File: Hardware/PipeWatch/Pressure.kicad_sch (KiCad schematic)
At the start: 4 parts, among them U6 ADS1115IDGS

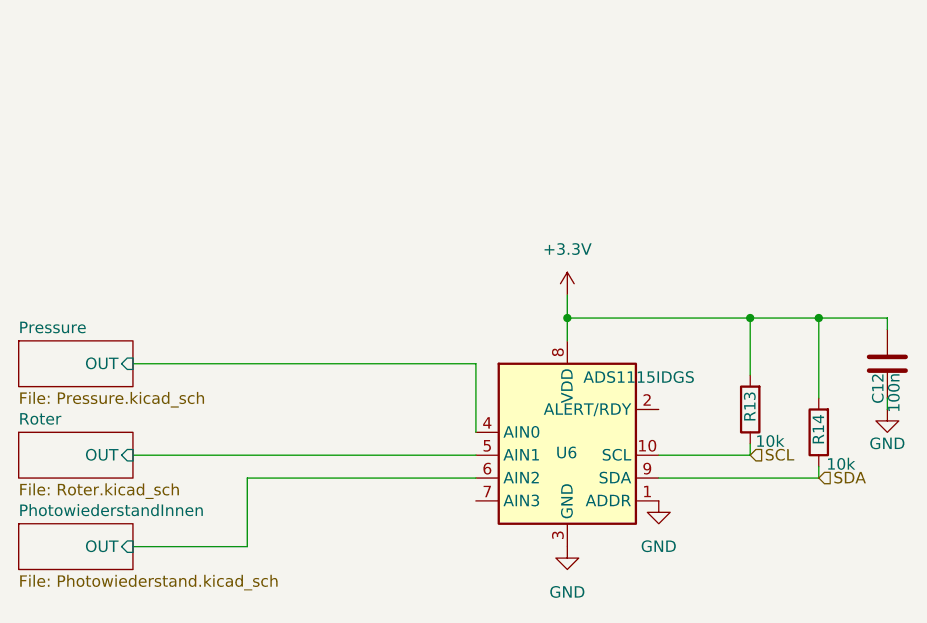
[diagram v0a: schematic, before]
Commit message: Started laying traces
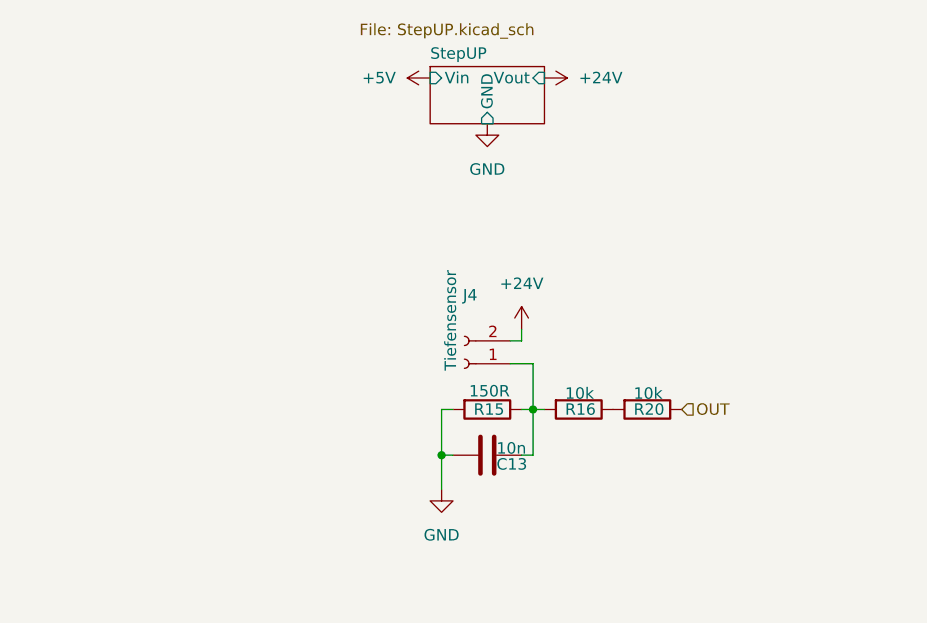
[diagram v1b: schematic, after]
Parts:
- removed C12: 100n, Capacitor_SMD:C_0603_1608Metric, symbol Device:C
- removed R13, R14: 10k, Resistor_SMD:R_0603_1608Metric, symbol Device:R
- removed U6: ADS1115IDGS, Package_SO:VSSOP-10_3x3mm_P0.5mm, symbol Analog_ADC:ADS1115IDGS
- added C13: 10n, Capacitor_SMD:C_0603_1608Metric, symbol Device:C
- added J4: Tiefensensor, Connector_PinSocket_2.54mm:PinSocket_1x02_P2.54mm_Vertical, symbol Connector:Conn_01x02_Socket
- added R15: 150R, Resistor_SMD:R_0805_2012Metric, symbol Device:R
- added R16, R20: 10k, Resistor_SMD:R_0603_1608Metric, symbol Device:R
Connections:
- net GND: now also C13.2, R15.2
- new net: C13.1, J4.1 (Pin_1), R15.1, R16.2
- new net: R16.1, R20.2
- new net +24V: J4.2 (Pin_2)
- new net OUT: R20.1
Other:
- removed sheet PhotowiederstandInnen
- removed sheet Pressure
- removed sheet Roter
- added sheet StepUP (StepUP.kicad_sch)

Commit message: Changed the scematic page Labeling
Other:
- company: (none) -> Felix Pelster
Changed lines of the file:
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@@
 	(generator_version "9.0")
 	(paper "A4")
+	(title_block
+		(date "2025-09-24")
+		(company "Felix Pelster")
+	)
 	(junction
 		(at 137.16 101.6)
